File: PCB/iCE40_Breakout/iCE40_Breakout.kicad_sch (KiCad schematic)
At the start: 0 parts

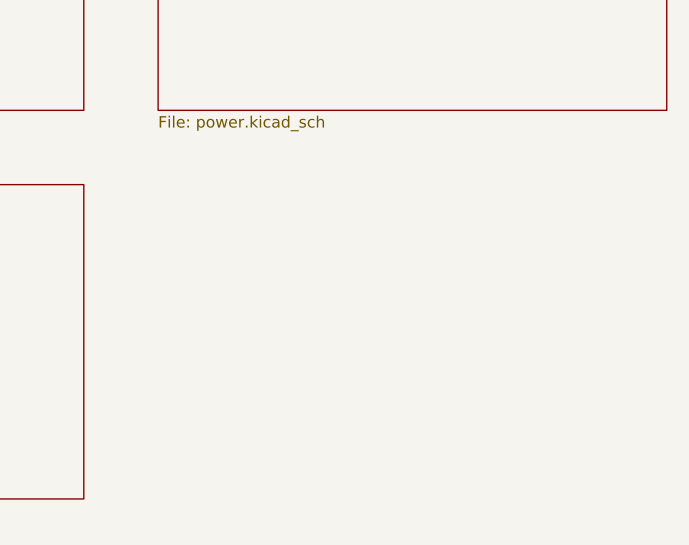
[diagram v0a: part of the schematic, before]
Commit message: Finished first draft of full schematic
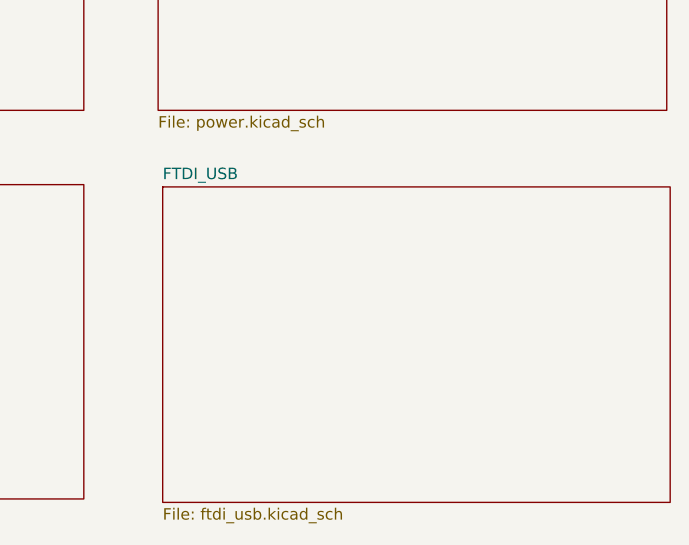
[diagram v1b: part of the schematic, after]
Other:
- added sheet FTDI_USB (ftdi_usb.kicad_sch)
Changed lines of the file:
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@@
+		)
+	)
+	(sheet
+		(at 104.648 72.644)
+		(size 56.388 35.052)
+		(exclude_from_sim no)
+		(in_bom yes)
+		(on_board yes)
+		(dnp no)
+		(fields_autoplaced yes)
+		(stroke
+			(width 0.1524)
+			(type solid)
+		)
+		(fill
+			(color 0 0 0 0.0000)
+		)
+		(property "Sheetname" "FTDI_USB"
+			(at 104.648 71.9324 0)
+			(effects
+				(font
+					(size 1.27 1.27)
+				)
+				(justify left bottom)
+			)
+		)
+		(property "Sheetfile" "ftdi_usb.kicad_sch"
+			(at 104.648 108.2806 0)
+			(effects
+				(font
+					(size 1.27 1.27)
+				)
+				(justify left top)
+			)
+		)
+		(instances
+			(project "iCE40_Breakout"
+				(path "/ce4d7974-ef38-4eea-8119-381c4298ef02"
+					(page "5")
+				)
+			)
 		)
 	)

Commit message: Added sheet information, and fixed ERC errors
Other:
- company: (none) -> S3I
- title: (none) -> iCE40 Breakout
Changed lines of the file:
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@@
 	(generator_version "9.0")
 	(paper "A4")
+	(title_block
+		(title "iCE40 Breakout")
+		(date "2025-11-26")
+		(rev "V1R0")
+		(company "S3I")
+		(comment 1 "Breakout board for the iCE40LP384, also testing flashing over USB using FTDI")
+	)
 	(sheet
 		(at 104.14 29.21)

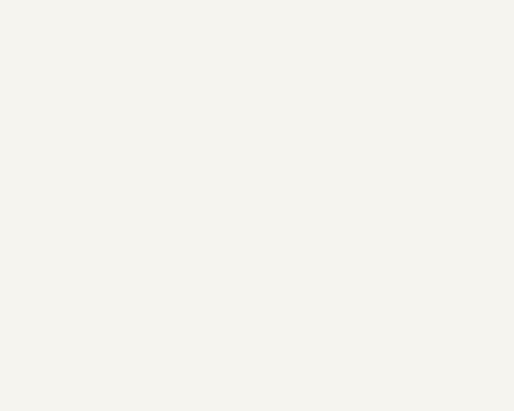
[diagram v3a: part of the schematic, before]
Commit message: Added mounting holes
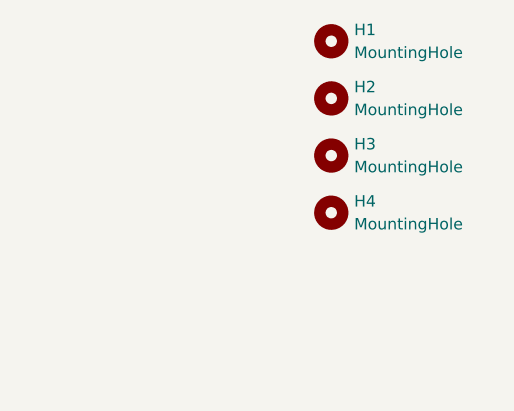
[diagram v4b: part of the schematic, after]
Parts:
- added H1, H2, H3, H4: MountingHole, MountingHole:MountingHole_2.2mm_M2, symbol Mechanical:MountingHole
